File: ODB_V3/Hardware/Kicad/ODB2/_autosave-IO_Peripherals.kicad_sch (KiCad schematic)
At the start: 31 parts, among them IC1 W25Q512JVEIQ, J11 Conn_02x04_Odd_Even, J2 RFD_GT17HN-4DP-2HA56, J3 SYS_SW_Conn_01x05_Header, J4 142-0701-801, J5 MEM2067, J6 IdeFIX_GT17HN-4DP-2HA56, U5 L76L-M33

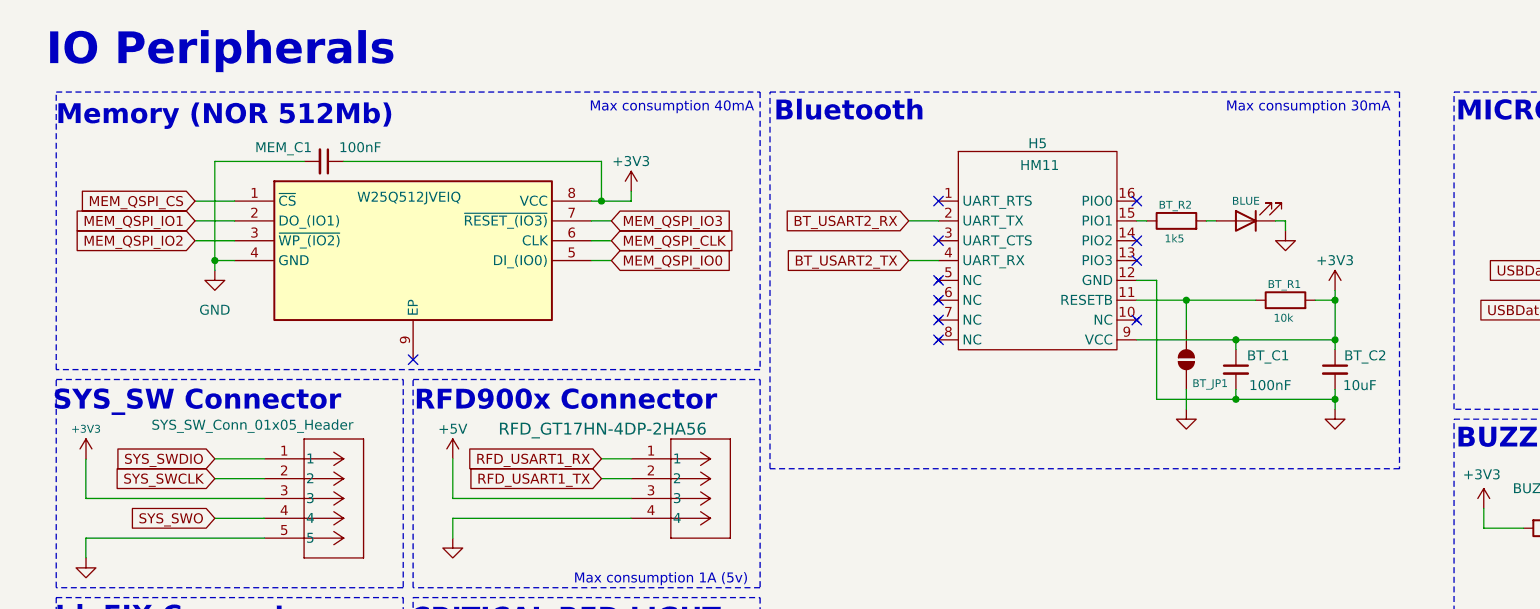
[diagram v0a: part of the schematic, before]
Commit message: wip: remove breakoutboard + add l76lm33 onboard
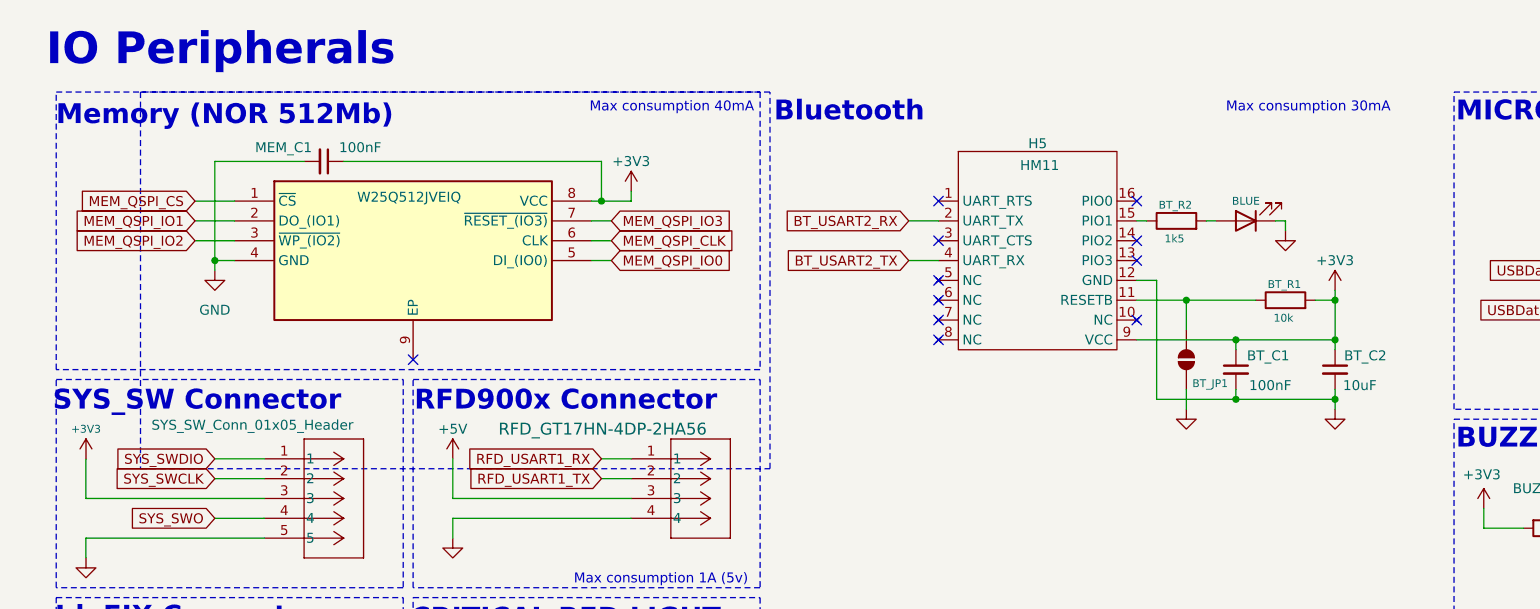
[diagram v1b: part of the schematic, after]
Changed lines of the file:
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@@
 	(rectangle
 		(start 105.41 21.59)
-		(end 186.055 69.85)
+		(end 24.765 69.85)
 		(stroke
 			(width 0)
